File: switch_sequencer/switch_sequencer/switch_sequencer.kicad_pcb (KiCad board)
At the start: 2 copper layers, 112 parts, among them J1 3.5mm_Mono_Switched_sm, J10 3.5mm_Mono_Switched_sm, J11 3.5mm_Mono_Switched_sm, J12 Conn_01x03, J14 Eurorack_Power_10pin_Shrouded, J2 3.5mm_Mono_Switched_sm, J3 3.5mm_Mono_Switched_sm, J4 3.5mm_Mono_Switched_sm, J5 3.5mm_Mono_Switched_sm, J6 3.5mm_Mono_Switched_sm, J7 3.5mm_Mono_Switched_sm, J8 3.5mm_Mono_Switched_sm, J9 3.5mm_Mono_Switched_sm, SW1 D6R90F2LFS, SW2 D6R90F2LFS, SW3 D6R90F2LFS, SW4 D6R90F2LFS, SW5 D6R90F2LFS, SW6 D6R90F2LFS, SW7 D6R90F2LFS, SW8 D6R90F2LFS, U1 TMUX4051PWR, U10 TL072, U11 TL072, U12 TL072, U13 TL072, U14 Pico, U3 LD1117S50TR_SOT223, U4 TL072, U5 TL072, U6 TL072, U7 TL072, U8 TL072, U9 TL072

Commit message: sequential swtich more wip
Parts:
- added C17: 100nF_0402_16V, 4ms_Capacitor:C_0402, F.Cu at (81.2, 55.8)
- added C18: 100nF_0402_16V, 4ms_Capacitor:C_0402, F.Cu at (81.3, 68.5)
- added C19: 100nF_0402_16V, 4ms_Capacitor:C_0402, F.Cu at (81.3, 81.2)
- added C20: 100nF_0402_16V, 4ms_Capacitor:C_0402, F.Cu at (81.3, 93.8)
- added C21: 100nF_0402_16V, 4ms_Capacitor:C_0402, F.Cu at (81.3, 106.5)
- added C22: 100nF_0402_16V, 4ms_Capacitor:C_0402, F.Cu at (81.3, 119.2)
- added C23: 100nF_0402_16V, 4ms_Capacitor:C_0402, F.Cu at (81.3, 131.9)
- added C24: 100nF_0402_16V, 4ms_Capacitor:C_0402, F.Cu at (144.6, 41.8)
- added C5: 0.1uF_0603_16V, 4ms_Capacitor:C_0603, F.Cu at (111.3, 51.2)
- added C6: 0.1uF_0603_16V, 4ms_Capacitor:C_0603, F.Cu at (114.8, 51.2)
- added C7: 0.1uF_0603_16V, 4ms_Capacitor:C_0603, F.Cu at (111.3, 53.0)
- added C8: 0.1uF_0603_16V, 4ms_Capacitor:C_0603, F.Cu at (114.8, 53.0)
- added FP1: Top Rail, 4ms_Faceplate:Rail_Connection_16HP, F.Cu at (81.8, 29.6)
- added FP2: Bottom Rail, 4ms_Faceplate:Rail_Connection_16HP, F.Cu at (81.8, 149.1)
- added Q1: DMG2305UX-7, DMG2305UX_7:SOT91P240X110-3N_DMG2305UX-7, F.Cu at (86.6, 132.4)
- added U2: LM4040DBZ-3, Package_TO_SOT_SMD:SOT-23, F.Cu at (86.9, 117.2)
- C10, C11, C12, C13, C14, C3, C4, C9: value 100nF_0402_16V -> 0.1uF_0603_16V; footprint 4ms_Capacitor:C_0402 -> 4ms_Capacitor:C_0603
- moved C15 103.2 mm to (144.6, 37.8)
- moved C16 88.9 mm to (81.3, 43.0)
- moved C14 58.8 mm to (114.8, 58.2)
- moved C3 46.9 mm to (111.3, 49.5)
- moved C13 46.6 mm to (111.3, 58.2)
- moved C12 41.6 mm to (114.8, 56.4)
- moved C4 37.5 mm to (114.8, 49.5)
- moved C10 33.5 mm to (114.8, 54.7)
- moved C11 32.3 mm to (111.3, 56.4)
- moved C9 32.2 mm to (111.3, 54.7)
- moved J14 11.9 mm to (113.1, 71.1)
- moved U3 5.08 mm to (98.9, 66.2)
- moved J12 3.23 mm to (119.3, 131.5)
- moved U14 2.01 mm to (103.4, 109.9)
- moved R14 1.67 mm to (58.7, 71.3), turned to -90 degrees
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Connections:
- C10 pad 1: 5V -> GNDA
- C10 pad 2: GND -> +12V
- C11 pad 1: 5V -> -12VA
- C11 pad 2: GND -> GNDA
- C12 pad 1: 5V -> GNDA
- C12 pad 2: GND -> +12V
- C13 pad 1: 5V -> -12VA
- C13 pad 2: GND -> GNDA
- C14 pad 1: 5V -> GNDA
- C14 pad 2: GND -> +12V
- C3 pad 1: 5V -> -12VA
- C3 pad 2: GND -> GNDA
- C4 pad 1: 5V -> GNDA
- C4 pad 2: GND -> +12V
- C9 pad 1: 5V -> -12VA
- C9 pad 2: GND -> GNDA
- J14 pad 4: GND -> GNDA
- J14 pad 6: GND -> GNDA
- J14 pad 8: GND -> GNDA
- U14 pad 11: BUTTON_4 -> unconnected-(U14-GPIO8-Pad11)
- U14 pad 12: BUTTON_5 -> unconnected-(U14-GPIO9-Pad12)
- U14 pad 14: BUTTON_6 -> unconnected-(U14-GPIO10-Pad14)
- U14 pad 15: BUTTON_7 -> unconnected-(U14-GPIO11-Pad15)
- U14 pad 16: BUTTON_8 -> unconnected-(U14-GPIO12-Pad16)
- U14 pad 25: unconnected-(U14-GPIO19-Pad25) -> BUTTON_5
- U14 pad 26: unconnected-(U14-GPIO20-Pad26) -> BUTTON_6
- U14 pad 27: unconnected-(U14-GPIO21-Pad27) -> BUTTON_7
- U14 pad 29: WS2812_SIG -> BUTTON_8
- U14 pad 39: unconnected-(U14-VSYS-Pad39) -> Net-(U14-VSYS)
- U14 pad 40: unconnected-(U14-VBUS-Pad40) -> Net-(U14-VBUS)
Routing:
- net 5V: track 177.9 -> 141.4 mm
- net /Clock Led/DOUT: track 19.6 -> 0.20 mm
- net unconnected-(U14-GPIO11-Pad15): track 0.00 -> 4.16 mm
- net /Clock Led/DIN: track 31.9 -> 28.8 mm
- net /Mux/Signal 6/LED_DOUT: track 11.8 -> 14.1 mm
- net /Mux/Signal 7/LED_DOUT: track 11.8 -> 14.0 mm
- net /Mux/Signal 4/LED_DOUT: track 11.8 -> 13.9 mm
- net /Mux/Signal 2/LED_DOUT: track 11.8 -> 13.9 mm
- net /Mux/Signal 3/LED_DOUT: track 11.9 -> 13.9 mm
- net /Mux/Signal 5/LED_DOUT: track 11.9 -> 13.9 mm
- net /Mux/IO_8: track 9.36 -> 8.16 mm
- net /Mux/IO_7: track 9.36 -> 8.16 mm
- net /Mux/IO_3: track 9.36 -> 8.16 mm
- net /Mux/IO_1: track 9.36 -> 8.16 mm
- net /Mux/IO_2: track 9.36 -> 8.16 mm
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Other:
- board outline added: 80.9 x 128.5 mm

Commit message: sequential switch wip more more
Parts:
- removed FP1: Top Rail, 4ms_Faceplate:Rail_Connection_16HP
- removed FP2: Bottom Rail, 4ms_Faceplate:Rail_Connection_16HP
- added C25: 100nF_0402_16V, 4ms_Capacitor:C_0402, F.Cu at (103.6, 81.3)
- added D20: WS2812B-2020, LED_SMD:LED_WS2812B-2020_PLCC4_2.0x2.0mm, F.Cu at (103.5, 78.9)
- added H1: MountingHole, 4ms_Faceplate:Faceplate_Rail_Mount_Slot_Plated, F.Cu at (48.9, 28.1)
- added H2: MountingHole, 4ms_Faceplate:Faceplate_Rail_Mount_Slot_Plated, F.Cu at (114.8, 28.1)
- added H3: MountingHole, 4ms_Faceplate:Faceplate_Rail_Mount_Slot_Plated, F.Cu at (48.9, 150.6)
- added H4: MountingHole, 4ms_Faceplate:Faceplate_Rail_Mount_Slot_Plated, F.Cu at (114.8, 150.6)
- added SW9: D6R90F2LFS, D6R90:D6R90_CNK, F.Cu at (96.5, 76.4)
- moved C15 46.0 mm to (99.4, 46.4), turned to 180 degrees
- moved C1 42.8 mm to (105.0, 63.9), turned to 0 degrees
- moved C2 42.8 mm to (105.0, 66.2), turned to 0 degrees
- moved C24 27.0 mm to (118.0, 46.4), turned to 180 degrees
- moved U2 6.46 mm to (86.6, 123.6)
- moved Q1 4.12 mm to (86.7, 136.5)
- moved U14 3.30 mm to (103.5, 113.2)
- moved J12 3.30 mm to (119.4, 134.8)
- moved C16 1.75 mm to (83.0, 43.0)
- moved C17 1.75 mm to (83.0, 55.8)
- moved C18 1.75 mm to (83.0, 68.5)
- moved C19 1.75 mm to (83.0, 81.2)
- moved C20 1.75 mm to (83.0, 93.8)
- moved C21 1.75 mm to (83.0, 106.5)
- moved C22 1.75 mm to (83.0, 119.2)
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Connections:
- C10 pad 1: GNDA -> GND
- C10 pad 2: +12V -> -12VA
- C11 pad 1: -12VA -> +12V
- C11 pad 2: GNDA -> GND
- C12 pad 1: GNDA -> GND
- C12 pad 2: +12V -> -12VA
- C13 pad 1: -12VA -> +12V
- C13 pad 2: GNDA -> GND
- C14 pad 1: GNDA -> GND
- C14 pad 2: +12V -> -12VA
- C3 pad 1: -12VA -> +12V
- C3 pad 2: GNDA -> GND
- C4 pad 1: GNDA -> GND
- C4 pad 2: +12V -> -12VA
- C5 pad 1: -12VA -> +12V
- C5 pad 2: GNDA -> GND
- C6 pad 1: GNDA -> GND
- C6 pad 2: +12V -> -12VA
- C7 pad 1: -12VA -> +12V
- C7 pad 2: GNDA -> GND
- C8 pad 1: GNDA -> GND
- C8 pad 2: +12V -> -12VA
- C9 pad 1: -12VA -> +12V
- C9 pad 2: GNDA -> GND
- D19 pad 3: WS2812_SIG -> /Mode Led/DOUT
- J10 pad 2: GNDA -> GND
- J10 pad 3: GNDA -> GND
- J11 pad 2: GNDA -> GND
- J11 pad 3: GNDA -> GND
- J14 pad 4: GNDA -> GND
- J14 pad 6: GNDA -> GND
- J14 pad 8: GNDA -> GND
- J3 pad 2: GNDA -> GND
- J3 pad 3: GNDA -> GND
- J4 pad 2: GNDA -> GND
- J4 pad 3: GNDA -> GND
- J5 pad 2: GNDA -> GND
- J5 pad 3: GNDA -> GND
- J6 pad 2: GNDA -> GND
- J6 pad 3: GNDA -> GND
- J7 pad 2: GNDA -> GND
- J7 pad 3: GNDA -> GND
- J8 pad 2: GNDA -> GND
- J8 pad 3: GNDA -> GND
- J9 pad 2: GNDA -> GND
- J9 pad 3: GNDA -> GND
- U10 pad 5: GNDA -> GND
- U11 pad 5: GNDA -> GND
- U12 pad 5: GNDA -> GND
- U13 pad 5: GNDA -> GND
- U14 pad 10: BUTTON_3 -> unconnected-(U14-GPIO7-Pad10)
- U14 pad 12: unconnected-(U14-GPIO9-Pad12) -> BUTTON_4
- U14 pad 14: unconnected-(U14-GPIO10-Pad14) -> BUTTON_3
- U14 pad 15: unconnected-(U14-GPIO11-Pad15) -> BUTTON_2
- U14 pad 16: unconnected-(U14-GPIO12-Pad16) -> BUTTON_1
- U14 pad 21: unconnected-(U14-GPIO16-Pad21) -> BUTTON_9
- U14 pad 22: unconnected-(U14-GPIO17-Pad22) -> WS2812_SIG
- U14 pad 31: CLOCK -> RESET
- U14 pad 32: RESET -> CLOCK
- U14 pad 7: BUTTON_1 -> unconnected-(U14-GPIO5-Pad7)_1
- U14 pad 9: BUTTON_2 -> unconnected-(U14-GPIO6-Pad9)_1
- U5 pad 5: GNDA -> GND
- U6 pad 5: GNDA -> GND
- U7 pad 5: GNDA -> GND
- U8 pad 5: GNDA -> GND
- U9 pad 5: GNDA -> GND
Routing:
- net +12V: track 8.37 -> 302.1 mm, vias 8 -> 11
- net -12VA: track 14.5 -> 279.7 mm, vias 8 -> 11
- net CLOCK: track 0.65 -> 146.3 mm, vias 0 -> 1
- net ADC_VREF: track 0.00 -> 135.3 mm, vias 0 -> 2
- net RESET: track 0.65 -> 129.6 mm, vias 0 -> 1
- net GNDA: track 0.00 -> 127.8 mm, vias 0 -> 4
- net BUTTON_1: track 0.00 -> 82.4 mm
- net /Mux/IO_8: track 8.16 -> 85.3 mm, vias 0 -> 2
- net BUTTON_2: track 0.00 -> 72.4 mm
- net /Mux/IO_7: track 8.16 -> 71.1 mm, vias 0 -> 2
- net BUTTON_3: track 0.00 -> 56.6 mm
- net /Mux/IO_6: track 8.16 -> 62.0 mm, vias 0 -> 2
- net BUTTON_4: track 0.00 -> 50.1 mm
- net 5V: track 141.4 -> 190.5 mm, vias 3 -> 4
- net MUX_D0: track 0.00 -> 45.8 mm, vias 0 -> 1
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- added copper zone on B.Cu, net GND
- added copper zone on F.Cu, net GND

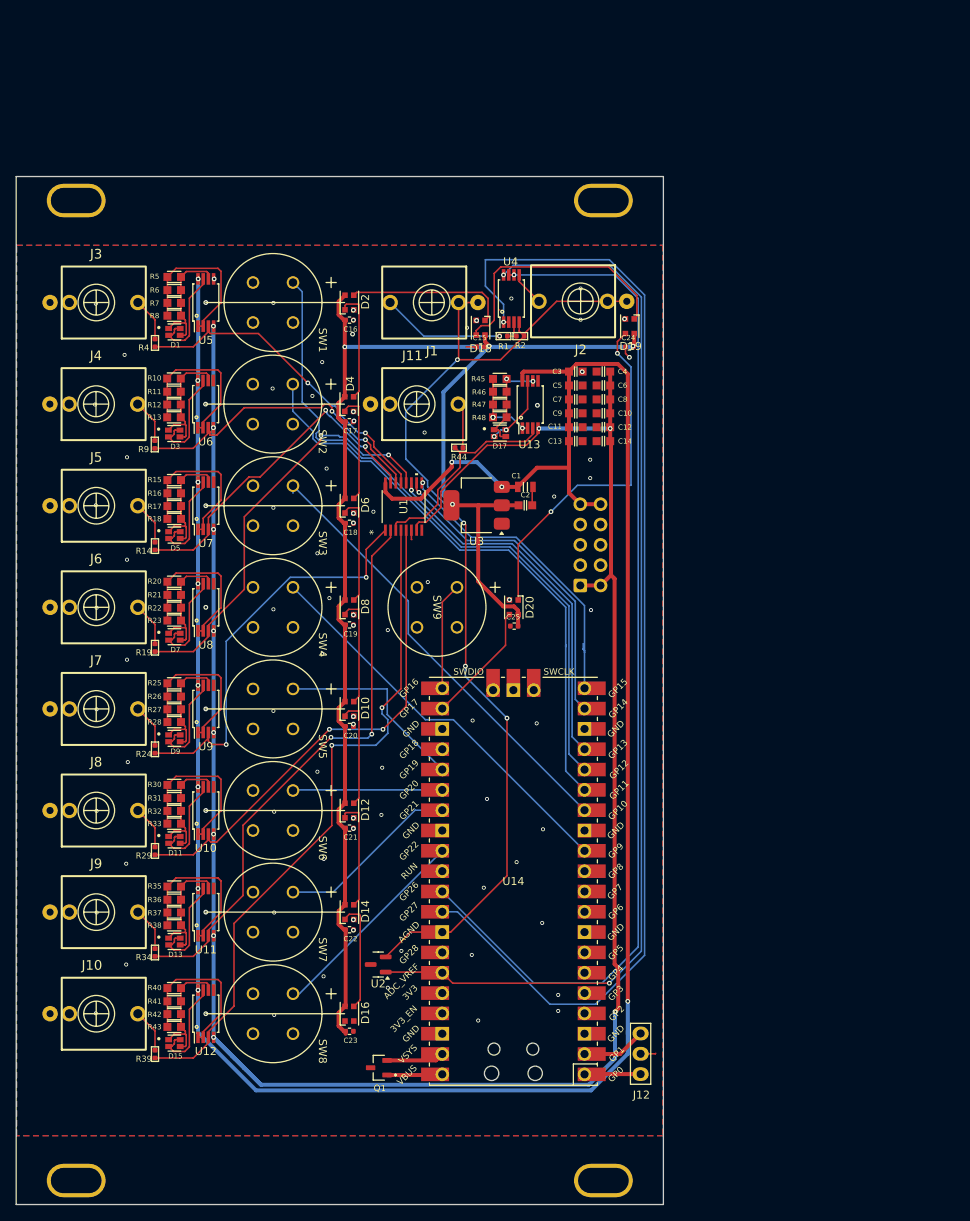
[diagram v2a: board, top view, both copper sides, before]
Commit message: sequential switch finished
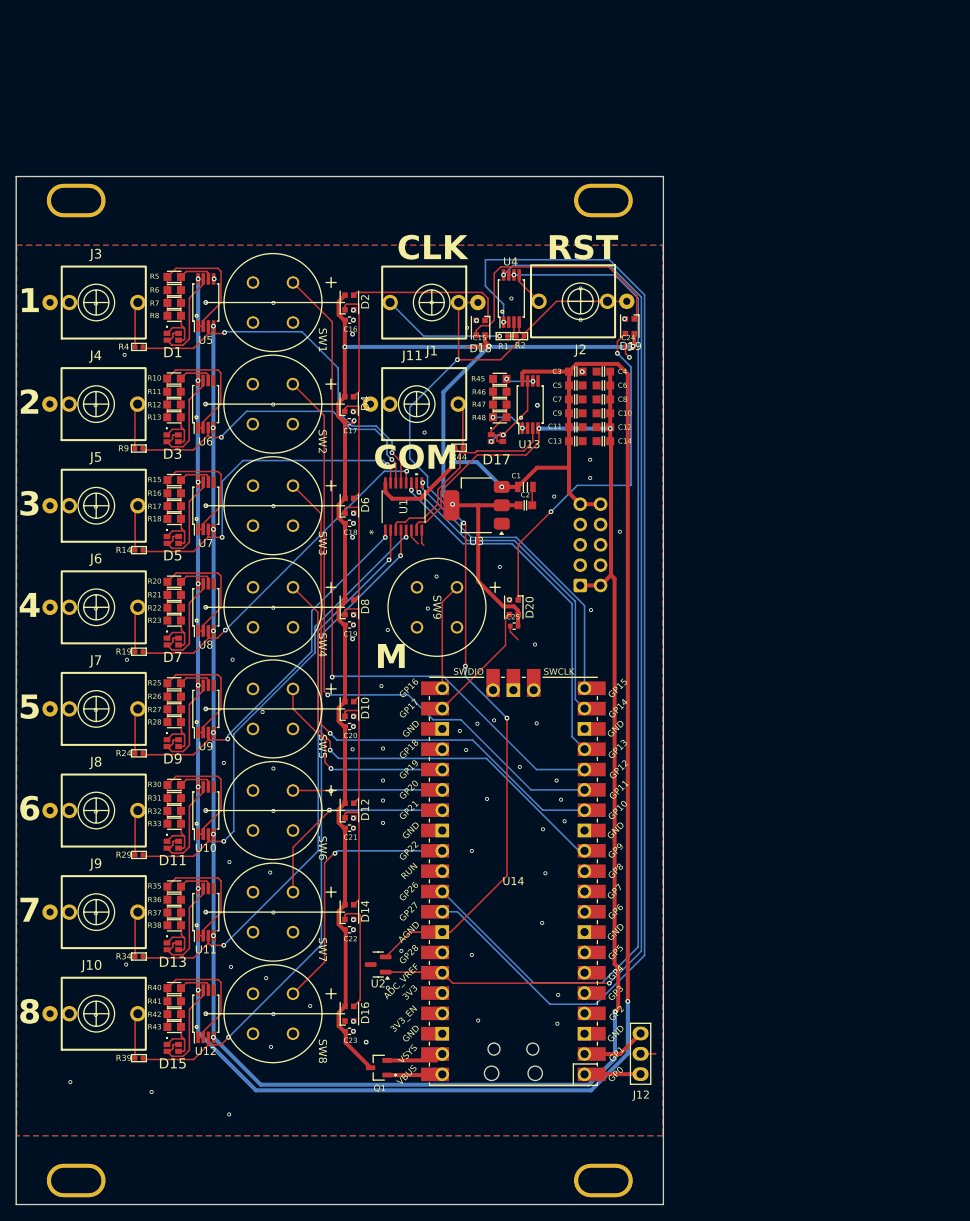
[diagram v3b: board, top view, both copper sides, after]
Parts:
- D1, D11, D13, D15, D17, D3, D5, D7, D9: footprint LTST-C195TBJRKT:LED_LTST-C195TBJRKT -> SamacSys_Parts:LTSTC195TBJRKT
- moved R14 2.06 mm to (56.7, 71.8), turned to 0 degrees
- moved R19 2.06 mm to (56.7, 84.5), turned to 0 degrees
- moved R24 2.06 mm to (56.7, 97.2), turned to 0 degrees
- moved R29 2.06 mm to (56.7, 109.9), turned to 0 degrees
- moved R34 2.06 mm to (56.7, 122.6), turned to 0 degrees
- moved R39 2.06 mm to (56.7, 135.3), turned to 0 degrees
- moved R4 2.06 mm to (56.7, 46.4), turned to 0 degrees
- moved R9 2.06 mm to (56.7, 59.1), turned to 0 degrees
- moved D17 0.73 mm to (101.4, 57.8), turned to 90 degrees
- moved D5 0.63 mm to (60.9, 70.5), turned to 90 degrees
- moved D3 0.63 mm to (60.9, 57.8), turned to 90 degrees
- moved D1 0.63 mm to (60.9, 45.1), turned to 90 degrees
- moved D13 0.63 mm to (60.9, 121.3), turned to 90 degrees
- moved D15 0.63 mm to (60.9, 134.0), turned to 90 degrees
- moved D11 0.63 mm to (60.9, 108.6), turned to 90 degrees
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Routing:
- net -12VA: track 279.7 -> 266.1 mm
- net BUTTON_3: track 56.6 -> 68.6 mm, vias 0 -> 1
- net BUTTON_4: track 50.1 -> 59.3 mm, vias 0 -> 1
- net /Mux/IO_1: track 41.4 -> 49.4 mm
- net BUTTON_8: track 26.1 -> 33.3 mm, vias 0 -> 1
- net /Mux/IO_4: track 52.3 -> 45.7 mm
- net GND: track 9.75 -> 16.3 mm, vias 89 -> 108
- net BUTTON_1: track 82.4 -> 87.8 mm, vias 0 -> 1
- net BUTTON_2: track 72.4 -> 77.7 mm, vias 0 -> 1
- net 5V: track 190.5 -> 195.7 mm
- net /Mux/IO_5: track 52.2 -> 47.5 mm
- net BUTTON_7: track 22.9 -> 26.2 mm, vias 0 -> 1
- net /Mux/Signal 6/LED_DOUT: track 14.1 -> 16.2 mm
- net /Mux/IO_2: track 39.2 -> 41.2 mm
- net /Mux/IO_7: track 71.1 -> 72.5 mm
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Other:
- board text added: "1"
- board text added: "2"
- board text added: "3"
- board text added: "4"
- board text added: "5"
- board text added: "6"
- board text added: "7"
- board text added: "8"
- board text added: "CLK"
- board text added: "COM"
- board text added: "M"
- board text added: "RST"

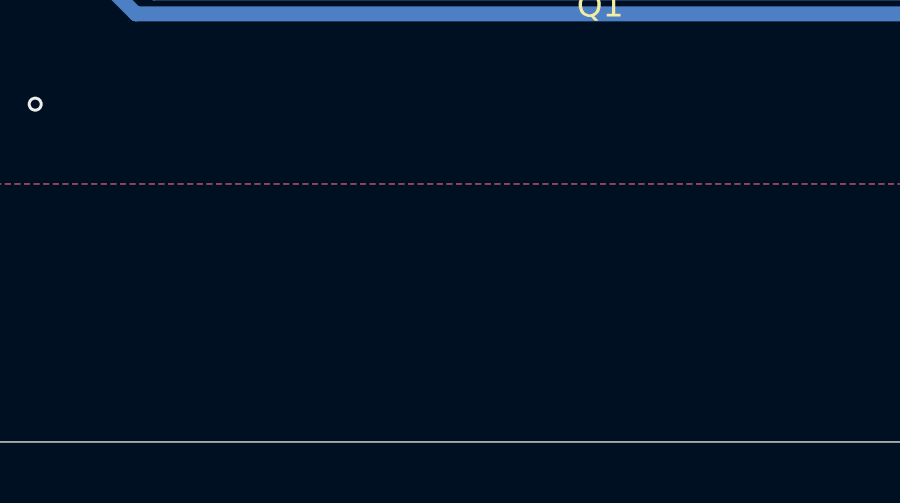
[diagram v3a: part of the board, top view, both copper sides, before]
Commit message: Added label to switch sequencer
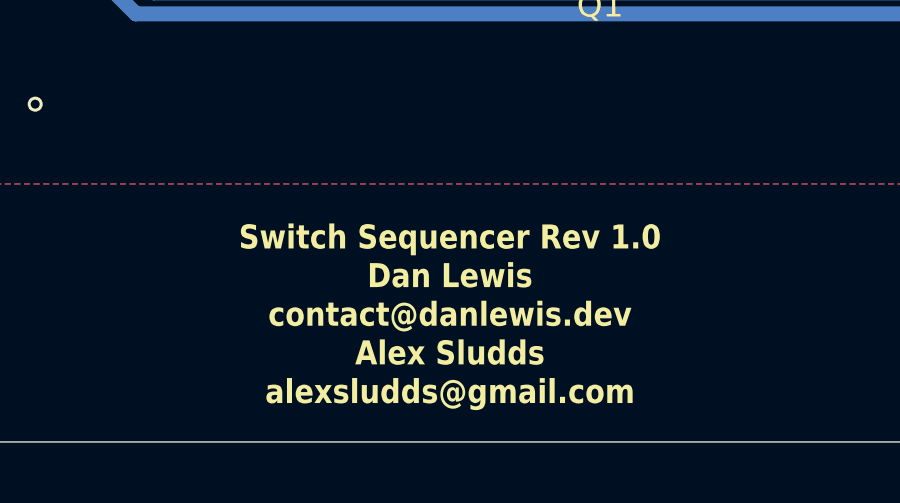
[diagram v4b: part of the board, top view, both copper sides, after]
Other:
- board text added: "Switch Sequencer Rev 1.0 Dan Lewis contact@danlewis.dev Alex Sludds alexsludds@gmail.com"
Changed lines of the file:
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@@
+		)
+	)
+	(gr_text "Switch Sequencer Rev 1.0\nDan Lewis\ncontact@danlewis.dev\nAlex Sludds\nalexsludds@gmail.com"
+		(at 81.8 152.4 0)
+		(layer "F.SilkS")
+		(effects
+			(font
+				(size 0.8 0.7)
+				(thickness 0.15)
+				(bold yes)
+			)
+			(justify bottom)
 		)
 	)
